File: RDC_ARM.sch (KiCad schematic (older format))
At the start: 38 parts, among them J1 RESOLVER ARM, Q1 BC807, Q2 BC807, U1 AD8397ARZ, X1 8.192MHz

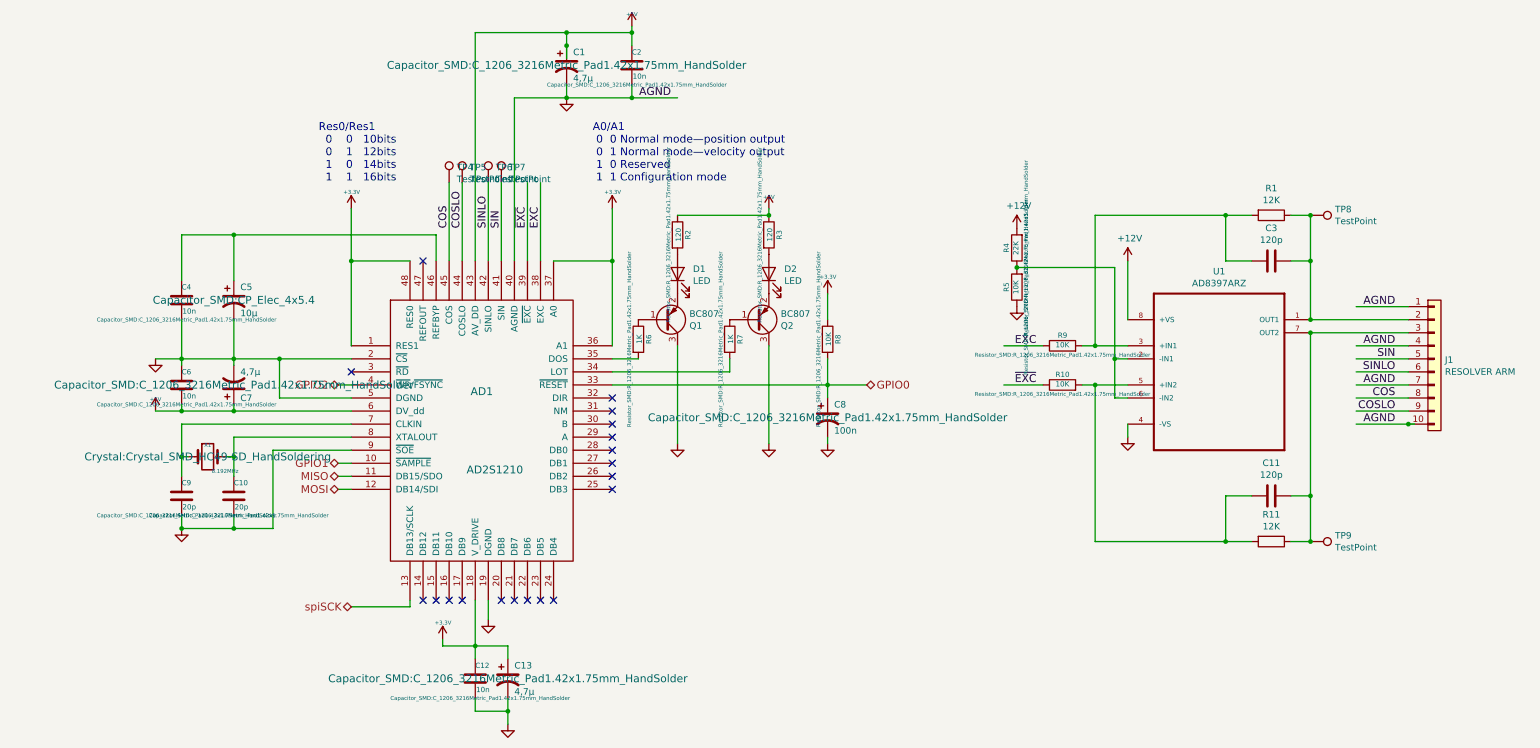
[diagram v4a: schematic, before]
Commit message: outline reducido, para revision por peers
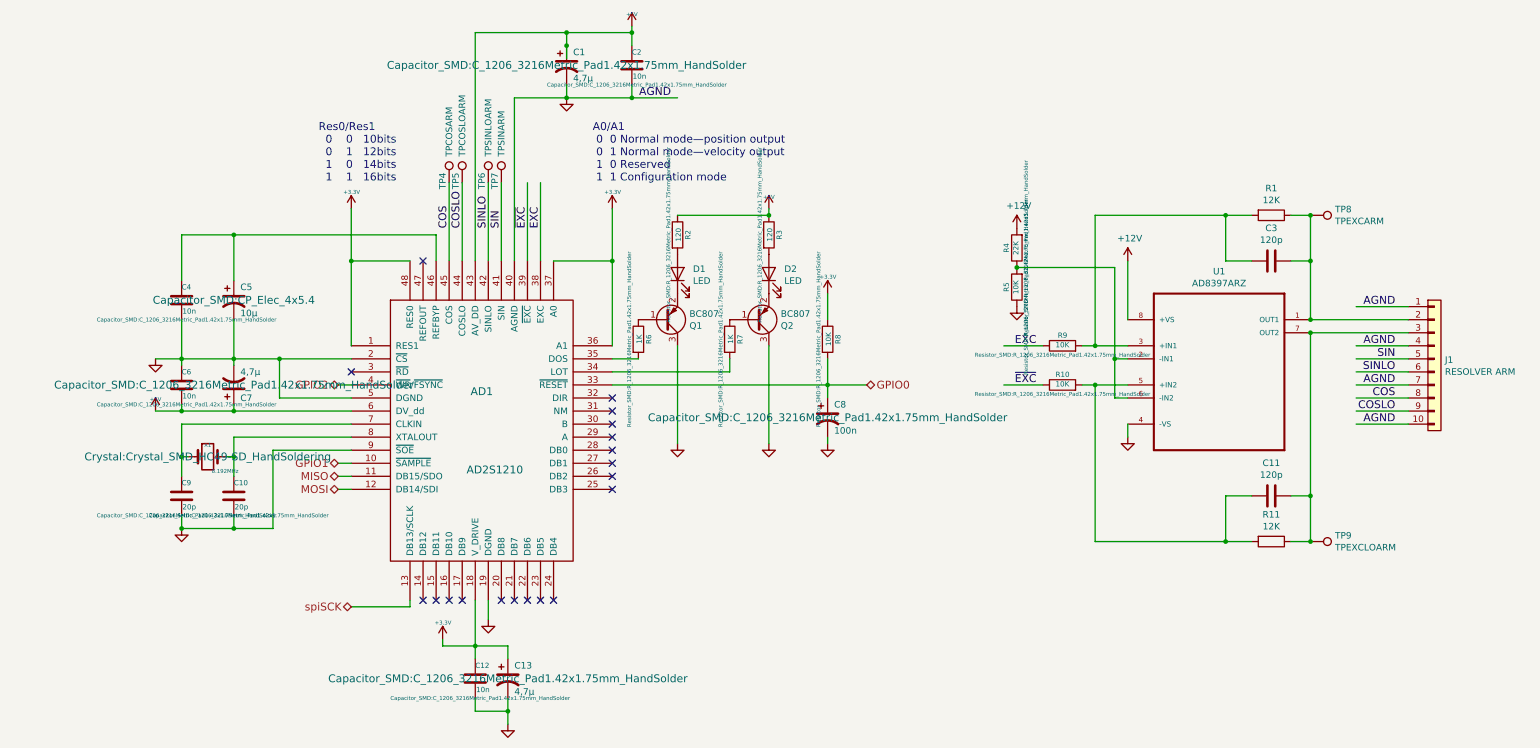
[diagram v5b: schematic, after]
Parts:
- TP4: value TestPoint -> TPCOSARM
- TP5: value TestPoint -> TPCOSLOARM
- TP6: value TestPoint -> TPSINLOARM
- TP7: value TestPoint -> TPSINARM
- TP8: value TestPoint -> TPEXCARM
- TP9: value TestPoint -> TPEXCLOARM
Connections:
- wire segments 131 -> 130
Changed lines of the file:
@@
 	9950 2950 9950 3300
+$Comp
+L Connector:TestPoint TP4
+U 1 1 5F0A4859
+P 3350 2700
+F 0 "TP4" V 3300 2650 50  0000 L CNN
+F 1 "TPCOSARM" V 3350 2900 50  0000 L CNN
+F 2 "TestPoint:TestPoint_THTPad_1.0x1.0mm_Drill0.5mm" H 3550 2700 50  0001 C CNN
+F 3 "~" H 3550 2700 50  0001 C CNN
+	1    3350 2700
+	1    0    0    -1
+$EndComp
+$Comp
+L Connector:TestPoint TP5
+U 1 1 5F0A6B93
+P 3450 2700
+F 0 "TP5" V 3400 2650 50  0000 L CNN
+F 1 "TPCOSLOARM" V 3450 2900 50  0000 L CNN
+F 2 "TestPoint:TestPoint_THTPad_1.0x1.0mm_Drill0.5mm" H 3650 2700 50  0001 C CNN
+F 3 "~" H 3650 2700 50  0001 C CNN
+	1    3450 2700
+	1    0    0    -1
+$EndComp
+$Comp
+L Connector:TestPoint TP6
+U 1 1 5F0A729F
+P 3650 2700
+F 0 "TP6" V 3600 2650 50  0000 L CNN
+F 1 "TPSINLOARM" V 3650 2900 50  0000 L CNN
+F 2 "TestPoint:TestPoint_THTPad_1.0x1.0mm_Drill0.5mm" H 3850 2700 50  0001 C CNN
+F 3 "~" H 3850 2700 50  0001 C CNN
+	1    3650 2700
+	1    0    0    -1
+$EndComp
+$Comp
+L Connector:TestPoint TP7
+U 1 1 5F0A7B14
+P 3750 2700
+F 0 "TP7" V 3700 2650 50  0000 L CNN
+F 1 "TPSINARM" V 3750 2900 50  0000 L CNN
+F 2 "TestPoint:TestPoint_THTPad_1.0x1.0mm_Drill0.5mm" H 3950 2700 50  0001 C CNN
+F 3 "~" H 3950 2700 50  0001 C CNN
+	1    3750 2700
+	1    0    0    -1
+$EndComp
+$Comp
+L Connector:TestPoint TP8
+U 1 1 5F0A9078
+P 9950 2950
+F 0 "TP8" V 9904 3138 50  0000 L CNN
+F 1 "TPEXCARM" V 9995 3138 50  0000 L CNN
+F 2 "TestPoint:TestPoint_THTPad_1.0x1.0mm_Drill0.5mm" H 10150 2950 50  0001 C CNN
+F 3 "~" H 10150 2950 50  0001 C CNN
+	1    9950 2950
+	0    1    1    0
+$EndComp
+Connection ~ 9950 2950
+$Comp
+L Connector:TestPoint TP9
+U 1 1 5F0A9A85
+P 9950 5450
+F 0 "TP9" V 9904 5638 50  0000 L CNN
+F 1 "TPEXCLOARM" V 9995 5638 50  0000 L CNN
+F 2 "TestPoint:TestPoint_THTPad_1.0x1.0mm_Drill0.5mm" H 10150 5450 50  0001 C CNN
+F 3 "~" H 10150 5450 50  0001 C CNN
+	1    9950 5450
+	0    1    1    0
+$EndComp
+Connection ~ 9950 5450
+Text Label 10600 4550 2    60   ~ 0
+AGND
+Wire Wire Line
+	9950 3750 10700 3750
+Connection ~ 9950 3750
+Wire Wire Line
+	9950 3850 10700 3850
+Connection ~ 9950 3850
+Wire Wire Line
+	10700 3650 10300 3650
+Text Label 10600 3650 2    60   ~ 0
+AGND
 $Comp
 L Connector_Generic:Conn_01x10 J1
@@
 $EndComp
 Wire Wire Line
-	10750 4550 10700 4550
-$Comp
-L Connector:TestPoint TP4
-U 1 1 5F0A4859
-P 3350 2700
-F 0 "TP4" H 3408 2818 50  0000 L CNN
-F 1 "TestPoint" H 3408 2727 50  0000 L CNN
-F 2 "TestPoint:TestPoint_THTPad_1.0x1.0mm_Drill0.5mm" H 3550 2700 50  0001 C CNN
-F 3 "~" H 3550 2700 50  0001 C CNN
-	1    3350 2700
-	1    0    0    -1
-$EndComp
-$Comp
-L Connector:TestPoint TP5
-U 1 1 5F0A6B93
-P 3450 2700
-F 0 "TP5" H 3508 2818 50  0000 L CNN
-F 1 "TestPoint" H 3508 2727 50  0000 L CNN
-F 2 "TestPoint:TestPoint_THTPad_1.0x1.0mm_Drill0.5mm" H 3650 2700 50  0001 C CNN
-F 3 "~" H 3650 2700 50  0001 C CNN
-	1    3450 2700
-	1    0    0    -1
-$EndComp
-$Comp
-L Connector:TestPoint TP6
-U 1 1 5F0A729F
-P 3650 2700
-F 0 "TP6" H 3708 2818 50  0000 L CNN
-F 1 "TestPoint" H 3708 2727 50  0000 L CNN
-F 2 "TestPoint:TestPoint_THTPad_1.0x1.0mm_Drill0.5mm" H 3850 2700 50  0001 C CNN
-F 3 "~" H 3850 2700 50  0001 C CNN
-	1    3650 2700
-	1    0    0    -1
-$EndComp
-$Comp
-L Connector:TestPoint TP7
-U 1 1 5F0A7B14
-P 3750 2700
-F 0 "TP7" H 3808 2818 50  0000 L CNN
-F 1 "TestPoint" H 3808 2727 50  0000 L CNN
-F 2 "TestPoint:TestPoint_THTPad_1.0x1.0mm_Drill0.5mm" H 3950 2700 50  0001 C CNN
-F 3 "~" H 3950 2700 50  0001 C CNN
-	1    3750 2700
-	1    0    0    -1
-$EndComp
-$Comp
-L Connector:TestPoint TP8
-U 1 1 5F0A9078
-P 9950 2950
-F 0 "TP8" V 9904 3138 50  0000 L CNN
-F 1 "TestPoint" V 9995 3138 50  0000 L CNN
-F 2 "TestPoint:TestPoint_THTPad_1.0x1.0mm_Drill0.5mm" H 10150 2950 50  0001 C CNN
-F 3 "~" H 10150 2950 50  0001 C CNN
-	1    9950 2950
-	0    1    1    0
-$EndComp
-Connection ~ 9950 2950
-$Comp
-L Connector:TestPoint TP9
-U 1 1 5F0A9A85
-P 9950 5450
-F 0 "TP9" V 9904 5638 50  0000 L CNN
-F 1 "TestPoint" V 9995 5638 50  0000 L CNN
-F 2 "TestPoint:TestPoint_THTPad_1.0x1.0mm_Drill0.5mm" H 10150 5450 50  0001 C CNN
-F 3 "~" H 10150 5450 50  0001 C CNN
-	1    9950 5450
-	0    1    1    0
-$EndComp
-Connection ~ 9950 5450
-Wire Wire Line
 	10700 4550 10300 4550
-Text Label 10600 4550 2    60   ~ 0
-AGND
-Connection ~ 10700 4550
-Wire Wire Line
-	9950 3750 10700 3750
-Connection ~ 9950 3750
-Wire Wire Line
-	9950 3850 10700 3850
-Connection ~ 9950 3850
-Wire Wire Line
-	10700 3650 10300 3650
-Text Label 10600 3650 2    60   ~ 0
-AGND
 $EndSCHEMATC

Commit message: cambiados capacitores electroliticos por tantalio (unpolarized). Agrandado footprint test pads, generado BOM, 35 vias
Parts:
- C1, C13, C7, C8: symbol Device:CP1 -> Device:C
- C5: footprint Capacitor_SMD:CP_Elec_4x5.4 -> Capacitor_SMD:C_1206_3216Metric_Pad1.42x1.75mm_HandSolder; symbol Device:CP1 -> Device:C
- TP4, TP5, TP6, TP7, TP8, TP9: footprint TestPoint:TestPoint_THTPad_1.0x1.0mm_Drill0.5mm -> TestPoint:TestPoint_THTPad_1.5x1.5mm_Drill0.7mm
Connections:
- wire segments 130 -> 129
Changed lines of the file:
@@
-$EndComp
-$Comp
-L Device:CP1 C?
-U 1 1 5F08F1DB
-P 4250 1800
-AR Path="/5F08F1DB" Ref="C?"  Part="1"
-AR Path="/5EF45E27/5F08F1DB" Ref="C1"  Part="1"
-AR Path="/5F077C82/5F08F1DB" Ref="C?"  Part="1"
-F 0 "C1" H 4300 1900 50  0000 L CNN
-F 1 "4,7µ" H 4300 1700 50  0000 L CNN
-F 2 "Capacitor_SMD:C_1206_3216Metric_Pad1.42x1.75mm_HandSolder" H 4250 1800 60  0000 C CNN
-F 3 "~" H 4250 1800 60  0000 C CNN
-	1    4250 1800
-	1    0    0    -1
 $EndComp
 $Comp
@@
 Text Label 5050 2050 2    60   ~ 0
 AGND
-Connection ~ 4250 1650
-Wire Wire Line
-	4250 1650 4250 1750
 $Comp
 L Device:R R?
@@
 NoConn ~ 3150 3300
 $Comp
-L Device:CP1 C?
-U 1 1 5EF52A3A
-P 3800 6500
-AR Path="/5EF52A3A" Ref="C?"  Part="1"
-AR Path="/5EF45E27/5EF52A3A" Ref="C13"  Part="1"
-AR Path="/5F077C82/5EF52A3A" Ref="C?"  Part="1"
-F 0 "C13" H 3850 6600 50  0000 L CNN
-F 1 "4,7µ" H 3850 6400 50  0000 L CNN
-F 2 "Capacitor_SMD:C_1206_3216Metric_Pad1.42x1.75mm_HandSolder" H 3800 6500 60  0000 C CNN
-F 3 "~" H 3800 6500 60  0000 C CNN
-	1    3800 6500
-	1    0    0    -1
-$EndComp
-$Comp
-L Device:CP1 C?
+L Device:C C?
 U 1 1 5EF539BB
 P 1700 4250
@@
 $EndComp
 $Comp
-L Device:CP1 C?
+L Device:C C?
 U 1 1 5F08F1CE
 P 1700 3600
@@
 F 0 "C5" H 1750 3700 50  0000 L CNN
 F 1 "10µ" H 1750 3500 50  0000 L CNN
-F 2 "Capacitor_SMD:CP_Elec_4x5.4" H 1700 3600 60  0000 C CNN
+F 2 "Capacitor_SMD:C_1206_3216Metric_Pad1.42x1.75mm_HandSolder" H 1700 3600 60  0000 C CNN
 F 3 "~" H 1700 3600 60  0000 C CNN
 	1    1700 3600
@@
 $EndComp
 $Comp
-L Device:CP1 C?
+L Device:C C?
 U 1 1 5EF555B8
 P 6250 4500
@@
 F 0 "TP4" V 3300 2650 50  0000 L CNN
 F 1 "TPCOSARM" V 3350 2900 50  0000 L CNN
-F 2 "TestPoint:TestPoint_THTPad_1.0x1.0mm_Drill0.5mm" H 3550 2700 50  0001 C CNN
+F 2 "TestPoint:TestPoint_THTPad_1.5x1.5mm_Drill0.7mm" H 3550 2700 50  0001 C CNN
 F 3 "~" H 3550 2700 50  0001 C CNN
 	1    3350 2700
@@
 F 0 "TP5" V 3400 2650 50  0000 L CNN
 F 1 "TPCOSLOARM" V 3450 2900 50  0000 L CNN
-F 2 "TestPoint:TestPoint_THTPad_1.0x1.0mm_Drill0.5mm" H 3650 2700 50  0001 C CNN
+F 2 "TestPoint:TestPoint_THTPad_1.5x1.5mm_Drill0.7mm" H 3650 2700 50  0001 C CNN
 F 3 "~" H 3650 2700 50  0001 C CNN
 	1    3450 2700
@@
 F 0 "TP6" V 3600 2650 50  0000 L CNN
 F 1 "TPSINLOARM" V 3650 2900 50  0000 L CNN
-F 2 "TestPoint:TestPoint_THTPad_1.0x1.0mm_Drill0.5mm" H 3850 2700 50  0001 C CNN
+F 2 "TestPoint:TestPoint_THTPad_1.5x1.5mm_Drill0.7mm" H 3850 2700 50  0001 C CNN
 F 3 "~" H 3850 2700 50  0001 C CNN
 	1    3650 2700
@@
 F 0 "TP7" V 3700 2650 50  0000 L CNN
 F 1 "TPSINARM" V 3750 2900 50  0000 L CNN
-F 2 "TestPoint:TestPoint_THTPad_1.0x1.0mm_Drill0.5mm" H 3950 2700 50  0001 C CNN
+F 2 "TestPoint:TestPoint_THTPad_1.5x1.5mm_Drill0.7mm" H 3950 2700 50  0001 C CNN
 F 3 "~" H 3950 2700 50  0001 C CNN
 	1    3750 2700
@@
 F 0 "TP8" V 9904 3138 50  0000 L CNN
 F 1 "TPEXCARM" V 9995 3138 50  0000 L CNN
-F 2 "TestPoint:TestPoint_THTPad_1.0x1.0mm_Drill0.5mm" H 10150 2950 50  0001 C CNN
+F 2 "TestPoint:TestPoint_THTPad_1.5x1.5mm_Drill0.7mm" H 10150 2950 50  0001 C CNN
 F 3 "~" H 10150 2950 50  0001 C CNN
 	1    9950 2950
@@
 F 0 "TP9" V 9904 5638 50  0000 L CNN
 F 1 "TPEXCLOARM" V 9995 5638 50  0000 L CNN
-F 2 "TestPoint:TestPoint_THTPad_1.0x1.0mm_Drill0.5mm" H 10150 5450 50  0001 C CNN
+F 2 "TestPoint:TestPoint_THTPad_1.5x1.5mm_Drill0.7mm" H 10150 5450 50  0001 C CNN
 F 3 "~" H 10150 5450 50  0001 C CNN
 	1    9950 5450
@@
 Wire Wire Line
 	10700 4550 10300 4550
+$Comp
+L Device:C C?
+U 1 1 5EF52A3A
+P 3800 6500
+AR Path="/5EF52A3A" Ref="C?"  Part="1"
+AR Path="/5EF45E27/5EF52A3A" Ref="C13"  Part="1"
+AR Path="/5F077C82/5EF52A3A" Ref="C?"  Part="1"
+F 0 "C13" H 3850 6600 50  0000 L CNN
+F 1 "4,7µ" H 3850 6400 50  0000 L CNN
+F 2 "Capacitor_SMD:C_1206_3216Metric_Pad1.42x1.75mm_HandSolder" H 3800 6500 60  0000 C CNN
+F 3 "~" H 3800 6500 60  0000 C CNN
+	1    3800 6500
+	1    0    0    -1
+$EndComp
+$Comp
+L Device:C C?
+U 1 1 5F08F1DB
+P 4250 1800
+AR Path="/5F08F1DB" Ref="C?"  Part="1"
+AR Path="/5EF45E27/5F08F1DB" Ref="C1"  Part="1"
+AR Path="/5F077C82/5F08F1DB" Ref="C?"  Part="1"
+F 0 "C1" H 4300 1900 50  0000 L CNN
+F 1 "4,7µ" H 4300 1700 50  0000 L CNN
+F 2 "Capacitor_SMD:C_1206_3216Metric_Pad1.42x1.75mm_HandSolder" H 4250 1800 60  0000 C CNN
+F 3 "~" H 4250 1800 60  0000 C CNN
+	1    4250 1800
+	1    0    0    -1
+$EndComp
 $EndSCHEMATC

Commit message: agrandados pads de test points
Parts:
- TP4, TP5, TP6, TP7, TP8, TP9: footprint TestPoint:TestPoint_THTPad_1.5x1.5mm_Drill0.7mm -> TestPoint:TestPoint_reducido
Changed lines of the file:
@@
 F 0 "TP4" V 3300 2650 50  0000 L CNN
 F 1 "TPCOSARM" V 3350 2900 50  0000 L CNN
-F 2 "TestPoint:TestPoint_THTPad_1.5x1.5mm_Drill0.7mm" H 3550 2700 50  0001 C CNN
+F 2 "TestPoint:TestPoint_reducido" H 3550 2700 50  0001 C CNN
 F 3 "~" H 3550 2700 50  0001 C CNN
 	1    3350 2700
@@
 F 0 "TP5" V 3400 2650 50  0000 L CNN
 F 1 "TPCOSLOARM" V 3450 2900 50  0000 L CNN
-F 2 "TestPoint:TestPoint_THTPad_1.5x1.5mm_Drill0.7mm" H 3650 2700 50  0001 C CNN
+F 2 "TestPoint:TestPoint_reducido" H 3650 2700 50  0001 C CNN
 F 3 "~" H 3650 2700 50  0001 C CNN
 	1    3450 2700
@@
 F 0 "TP6" V 3600 2650 50  0000 L CNN
 F 1 "TPSINLOARM" V 3650 2900 50  0000 L CNN
-F 2 "TestPoint:TestPoint_THTPad_1.5x1.5mm_Drill0.7mm" H 3850 2700 50  0001 C CNN
+F 2 "TestPoint:TestPoint_reducido" H 3850 2700 50  0001 C CNN
 F 3 "~" H 3850 2700 50  0001 C CNN
 	1    3650 2700
@@
 F 0 "TP7" V 3700 2650 50  0000 L CNN
 F 1 "TPSINARM" V 3750 2900 50  0000 L CNN
-F 2 "TestPoint:TestPoint_THTPad_1.5x1.5mm_Drill0.7mm" H 3950 2700 50  0001 C CNN
+F 2 "TestPoint:TestPoint_reducido" H 3950 2700 50  0001 C CNN
 F 3 "~" H 3950 2700 50  0001 C CNN
 	1    3750 2700
@@
 F 0 "TP8" V 9904 3138 50  0000 L CNN
 F 1 "TPEXCARM" V 9995 3138 50  0000 L CNN
-F 2 "TestPoint:TestPoint_THTPad_1.5x1.5mm_Drill0.7mm" H 10150 2950 50  0001 C CNN
+F 2 "TestPoint:TestPoint_reducido" H 10150 2950 50  0001 C CNN
 F 3 "~" H 10150 2950 50  0001 C CNN
 	1    9950 2950
@@
 F 0 "TP9" V 9904 5638 50  0000 L CNN
 F 1 "TPEXCLOARM" V 9995 5638 50  0000 L CNN
-F 2 "TestPoint:TestPoint_THTPad_1.5x1.5mm_Drill0.7mm" H 10150 5450 50  0001 C CNN
+F 2 "TestPoint:TestPoint_reducido" H 10150 5450 50  0001 C CNN
 F 3 "~" H 10150 5450 50  0001 C CNN
 	1    9950 5450
